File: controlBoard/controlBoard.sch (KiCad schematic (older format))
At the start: 18 parts, among them J1 FTDI, J2 Servo, J3 Fingerprint, J4 Barrel_Jack_Switch_MountingPin, J5 ICSP, SW1 SW_Push, SW2 SW_Push, SW3 SW_Push, U4 ATmega328P-AU, U5 PCA9685BS, Y1 Crystal

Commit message: Added button footprint and layout pcb
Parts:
- removed R1, R2: 10k, Resistor_SMD:R_0805_2012Metric_Pad1.20x1.40mm_HandSolder, symbol device:R_Small
- added C1, C2: 100n, Capacitor_SMD:C_0805_2012Metric_Pad1.18x1.45mm_HandSolder, symbol Device:C_Small
- added JP1: JVCC, Jumper:SolderJumper-2_P1.3mm_Open_RoundedPad1.0x1.5mm, symbol Jumper:SolderJumper_2_Open
- C3: renamed from C1; symbol device:C_Small -> controlBoard-rescue:C_Small-device
- C4: renamed from C2; symbol device:C_Small -> controlBoard-rescue:C_Small-device
- C5: renamed from C3; symbol device:C_Small -> controlBoard-rescue:C_Small-device
- C6: renamed from C4; symbol device:C_Small -> controlBoard-rescue:C_Small-device
- J3: footprint Connector_PinHeader_2.54mm:PinHeader_1x06_P2.54mm_Vertical -> Connector_JST:JST_PH_B6B-PH-K_1x06_P2.00mm_Vertical
- R3: renamed from R5; symbol device:R_Small -> controlBoard-rescue:R_Small-device
- SW1, SW2, SW3: footprint (none) -> bidpl:SMD_Pushbutton_3mmx4mm
- U1: renamed from U4; symbol MCU_Microchip_ATmega:ATmega328P-AU -> controlBoard-rescue:ATmega328P-AU-MCU_Microchip_ATmega
- Y1: footprint Crystal:Crystal_SMD_HC49-SD_HandSoldering -> Crystal:Crystal_SMD_5032-2Pin_5.0x3.2mm_HandSoldering; symbol device:Crystal -> controlBoard-rescue:Crystal-device
- renumbered U5 to U2
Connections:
- wire segments 96 -> 108

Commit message: Swapped TX1 and RX1 pins, cleaned up board a bit to send off to production
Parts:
- C1, C2: symbol Device:C_Small -> controlBoard-rescue:C_Small-Device
- J1, J3: symbol Connector_Generic:Conn_01x06 -> controlBoard-rescue:Conn_01x06-Connector_Generic
- J2: symbol Connector_Generic:Conn_01x03 -> controlBoard-rescue:Conn_01x03-Connector_Generic
- J4: symbol Connector:Barrel_Jack_Switch_MountingPin -> controlBoard-rescue:Barrel_Jack_Switch_MountingPin-Connector
- J5: symbol Connector_Generic:Conn_02x03_Odd_Even -> controlBoard-rescue:Conn_02x03_Odd_Even-Connector_Generic
- JP1: symbol Jumper:SolderJumper_2_Open -> controlBoard-rescue:SolderJumper_2_Open-Jumper
- SW1, SW2, SW3: symbol Switch:SW_Push -> controlBoard-rescue:SW_Push-Switch
- U2: symbol Driver_LED:PCA9685BS -> controlBoard-rescue:PCA9685BS-Driver_LED
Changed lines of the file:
@@
 $EndComp
 $Comp
-L power:GND #PWR017
+L controlBoard-rescue:GND-power #PWR017
 U 1 1 618DE613
 P 4200 5400
@@
 	4200 5300 4200 5400
 $Comp
-L power:+5V #PWR016
+L controlBoard-rescue:+5V-power #PWR016
 U 1 1 618E0ABB
 P 4200 2200
@@
 Connection ~ 4300 2250
 $Comp
-L power:GND #PWR018
+L controlBoard-rescue:GND-power #PWR018
 U 1 1 618E518F
 P 4800 2300
@@
 $EndComp
 $Comp
-L power:+5V #PWR019
+L controlBoard-rescue:+5V-power #PWR019
 U 1 1 618E816C
 P 5350 3750
@@
 	5350 4100 4800 4100
 $Comp
-L Switch:SW_Push SW3
+L controlBoard-rescue:SW_Push-Switch SW3
 U 1 1 618E9B97
 P 5900 4100
@@
 $EndComp
 $Comp
-L power:GND #PWR021
+L controlBoard-rescue:GND-power #PWR021
 U 1 1 618EA8D6
 P 6150 4150
@@
 	5850 3450 5650 3450
 $Comp
-L power:GND #PWR020
+L controlBoard-rescue:GND-power #PWR020
 U 1 1 618F026E
 P 5850 3550
@@
 	7700 4800 7700 4850
 $Comp
-L power:GND #PWR025
+L controlBoard-rescue:GND-power #PWR025
 U 1 1 618FA727
 P 7700 4900
@@
 Connection ~ 7700 4850
 $Comp
-L power:+5V #PWR024
+L controlBoard-rescue:+5V-power #PWR024
 U 1 1 618FB6AB
 P 7700 2600
@@
 	7700 2650 7700 2700
 $Comp
-L power:GND #PWR026
+L controlBoard-rescue:GND-power #PWR026
 U 1 1 61901090
 P 8300 2700
@@
 $EndComp
 $Comp
-L Driver_LED:PCA9685BS U2
+L controlBoard-rescue:PCA9685BS-Driver_LED U2
 U 1 1 618F6082
 P 7700 3700
@@
 F 1 "PCA9685BS" H 7400 4550 50  0000 C CNN
 F 2 "Package_DFN_QFN:QFN-28-1EP_6x6mm_P0.65mm_EP4.25x4.25mm" H 7725 2725 50  0001 L CNN
-F 3 "http://www.nxp.com/documents/data_sheet/PCA9685.pdf" H 7300 4400 50  0001 C CNN
+F 3 "https://www.nxp.com/docs/en/data-sheet/PCA9685.pdf" H 7300 4400 50  0001 C CNN
 	1    7700 3700
 	1    0    0    -1
@@
 	8300 2650 8300 2700
 $Comp
-L Switch:SW_Push SW1
+L controlBoard-rescue:SW_Push-Switch SW1
 U 1 1 6191D17B
 P 1350 5700
@@
 $EndComp
 $Comp
-L Switch:SW_Push SW2
+L controlBoard-rescue:SW_Push-Switch SW2
 U 1 1 6191DBBE
 P 1350 6750
@@
 $EndComp
 $Comp
-L power:GND #PWR08
+L controlBoard-rescue:GND-power #PWR08
 U 1 1 61922AC3
 P 1050 6850
@@
 $EndComp
 $Comp
-L power:GND #PWR07
+L controlBoard-rescue:GND-power #PWR07
 U 1 1 61922CB3
 P 1050 5800
@@
 $EndComp
 $Comp
-L Connector:Barrel_Jack_Switch_MountingPin J4
+L controlBoard-rescue:Barrel_Jack_Switch_MountingPin-Connector J4
 U 1 1 618E34A5
 P 1300 1150
@@
 $EndComp
 $Comp
-L Connector_Generic:Conn_02x03_Odd_Even J5
+L controlBoard-rescue:Conn_02x03_Odd_Even-Connector_Generic J5
 U 1 1 618EA8EC
 P 2450 2300
@@
 $EndComp
 $Comp
-L Connector_Generic:Conn_01x03 J2
+L controlBoard-rescue:Conn_01x03-Connector_Generic J2
 U 1 1 618ECDBF
 P 1050 3300
@@
 $EndComp
 $Comp
-L power:GND #PWR011
+L controlBoard-rescue:GND-power #PWR011
 U 1 1 618F500B
 P 1850 1500
@@
 	1600 1250 1850 1250
 $Comp
-L power:+5V #PWR012
+L controlBoard-rescue:+5V-power #PWR012
 U 1 1 619089DF
 P 2000 1000
@@
 	2000 1050 2000 1000
 $Comp
-L power:+5V #PWR013
+L controlBoard-rescue:+5V-power #PWR013
 U 1 1 6192E22C
 P 2800 2150
@@
 $EndComp
 $Comp
-L power:GND #PWR014
+L controlBoard-rescue:GND-power #PWR014
 U 1 1 6192F1F2
 P 2800 2450
@@
 	1250 3200 1600 3200
 $Comp
-L power:GND #PWR04
+L controlBoard-rescue:GND-power #PWR04
 U 1 1 61955E60
 P 1300 3450
@@
 	1300 3400 1300 3450
 $Comp
-L power:+5V #PWR010
+L controlBoard-rescue:+5V-power #PWR010
 U 1 1 61959E6E
 P 1750 3250
@@
 Text Label 8450 3000 0    50   ~ 0
 PWM0
-$Comp
-L Connector_Generic:Conn_01x06 J3
-U 1 1 61962843
-P 1050 4200
-F 0 "J3" H 968 4617 50  0000 C CNN
-F 1 "Fingerprint" H 968 4526 50  0000 C CNN
-F 2 "Connector_JST:JST_PH_B6B-PH-K_1x06_P2.00mm_Vertical" H 1050 4200 50  0001 C CNN
-F 3 "~" H 1050 4200 50  0001 C CNN
-	1    1050 4200
-	-1   0    0    -1
-$EndComp
-Wire Wire Line
-	1250 4400 1400 4400
-Wire Wire Line
-	1250 4300 1400 4300
-Wire Wire Line
-	1250 4200 1400 4200
-Wire Wire Line
-	1400 4200 1400 4150
-Wire Wire Line
-	1250 4500 1400 4500
-Wire Wire Line
-	1400 4500 1400 4550
-$Comp
-L power:GND #PWR06
-U 1 1 6197312B
-P 1400 4550
-F 0 "#PWR06" H 1400 4300 50  0001 C CNN
-F 1 "GND" H 1405 4377 50  0000 C CNN
-F 2 "" H 1400 4550 50  0001 C CNN
-F 3 "" H 1400 4550 50  0001 C CNN
-	1    1400 4550
-	1    0    0    -1
-$EndComp
-$Comp
-L power:+5V #PWR05
-U 1 1 61973A8E
-P 1400 4150
-F 0 "#PWR05" H 1400 4000 50  0001 C CNN
-F 1 "+5V" H 1415 4323 50  0000 C CNN
-F 2 "" H 1400 4150 50  0001 C CNN
-F 3 "" H 1400 4150 50  0001 C CNN
-	1    1400 4150
-	1    0    0    -1
-$EndComp
-Text Label 1250 4400 0    50   ~ 0
-RX1
-Text Label 1250 4300 0    50   ~ 0
-TX1
-NoConn ~ 1250 4100
-NoConn ~ 1250 4000
 Wire Wire Line
 	4800 4500 5000 4500
@@
 	4800 4600 5000 4600
 Text Label 4850 4500 0    50   ~ 0
+TX1
+Text Label 4850 4600 0    50   ~ 0
 RX1
-Text Label 4850 4600 0    50   ~ 0
-TX1
-$Comp
-L power:GND #PWR03
+$Comp
+L controlBoard-rescue:GND-power #PWR03
 U 1 1 6199143D
 P 1300 2750
@@
 RX
 $Comp
-L power:+5V #PWR09
+L controlBoard-rescue:+5V-power #PWR09
 U 1 1 6199F7F4
 P 1750 2450
@@
 	6800 3900 6800 4000
 $Comp
-L power:GND #PWR022
+L controlBoard-rescue:GND-power #PWR022
 U 1 1 61BB2179
 P 6800 4500
@@
 	6950 4400 7000 4400
 $Comp
-L power:+5V #PWR023
+L controlBoard-rescue:+5V-power #PWR023
 U 1 1 61BD1C2C
 P 6950 4400
@@
 $EndComp
 $Comp
-L Jumper:SolderJumper_2_Open JP1
+L controlBoard-rescue:SolderJumper_2_Open-Jumper JP1
 U 1 1 61BD91B4
 P 1550 2500
@@
 	1250 2500 1400 2500
 $Comp
-L Device:C_Small C1
+L controlBoard-rescue:C_Small-Device C1
 U 1 1 61BF76F9
 P 1500 2200
@@
 	1750 2500 1750 2450
 $Comp
-L Device:C_Small C2
+L controlBoard-rescue:C_Small-Device C2
 U 1 1 61C0D1ED
 P 3400 2600
@@
 $EndComp
 $Comp
-L power:GND #PWR015
+L controlBoard-rescue:GND-power #PWR015
 U 1 1 61C0E312
 P 3200 2700
@@
 	3200 2600 3300 2600
 $Comp
-L Connector_Generic:Conn_01x06 J1
+L controlBoard-rescue:Conn_01x06-Connector_Generic J1
 U 1 1 618EBBB2
 P 1050 2500
@@
 Wire Wire Line
 	1050 6750 1050 6850
+NoConn ~ 1250 4000
+NoConn ~ 1250 4100
+Text Label 1250 4300 0    50   ~ 0
+TX1
+Text Label 1250 4400 0    50   ~ 0
+RX1
+$Comp
+L controlBoard-rescue:+5V-power #PWR05
+U 1 1 61973A8E
+P 1400 4150
+F 0 "#PWR05" H 1400 4000 50  0001 C CNN
+F 1 "+5V" H 1415 4323 50  0000 C CNN
+F 2 "" H 1400 4150 50  0001 C CNN
+F 3 "" H 1400 4150 50  0001 C CNN
+	1    1400 4150
+	1    0    0    -1
+$EndComp
+$Comp
+L controlBoard-rescue:GND-power #PWR06
+U 1 1 6197312B
+P 1400 4550
+F 0 "#PWR06" H 1400 4300 50  0001 C CNN
+F 1 "GND" H 1405 4377 50  0000 C CNN
+F 2 "" H 1400 4550 50  0001 C CNN
+F 3 "" H 1400 4550 50  0001 C CNN
+	1    1400 4550
+	1    0    0    -1
+$EndComp
+Wire Wire Line
+	1400 4500 1400 4550
+Wire Wire Line
+	1250 4500 1400 4500
+Wire Wire Line
+	1400 4200 1400 4150
+Wire Wire Line
+	1250 4200 1400 4200
+Wire Wire Line
+	1250 4300 1400 4300
+Wire Wire Line
+	1250 4400 1400 4400
+$Comp
+L controlBoard-rescue:Conn_01x06-Connector_Generic J3
+U 1 1 61962843
+P 1050 4200
+F 0 "J3" H 968 4617 50  0000 C CNN
+F 1 "Fingerprint" H 968 4526 50  0000 C CNN
+F 2 "Connector_JST:JST_PH_B6B-PH-K_1x06_P2.00mm_Vertical" H 1050 4200 50  0001 C CNN
+F 3 "~" H 1050 4200 50  0001 C CNN
+	1    1050 4200
+	-1   0    0    -1
+$EndComp
 $EndSCHEMATC

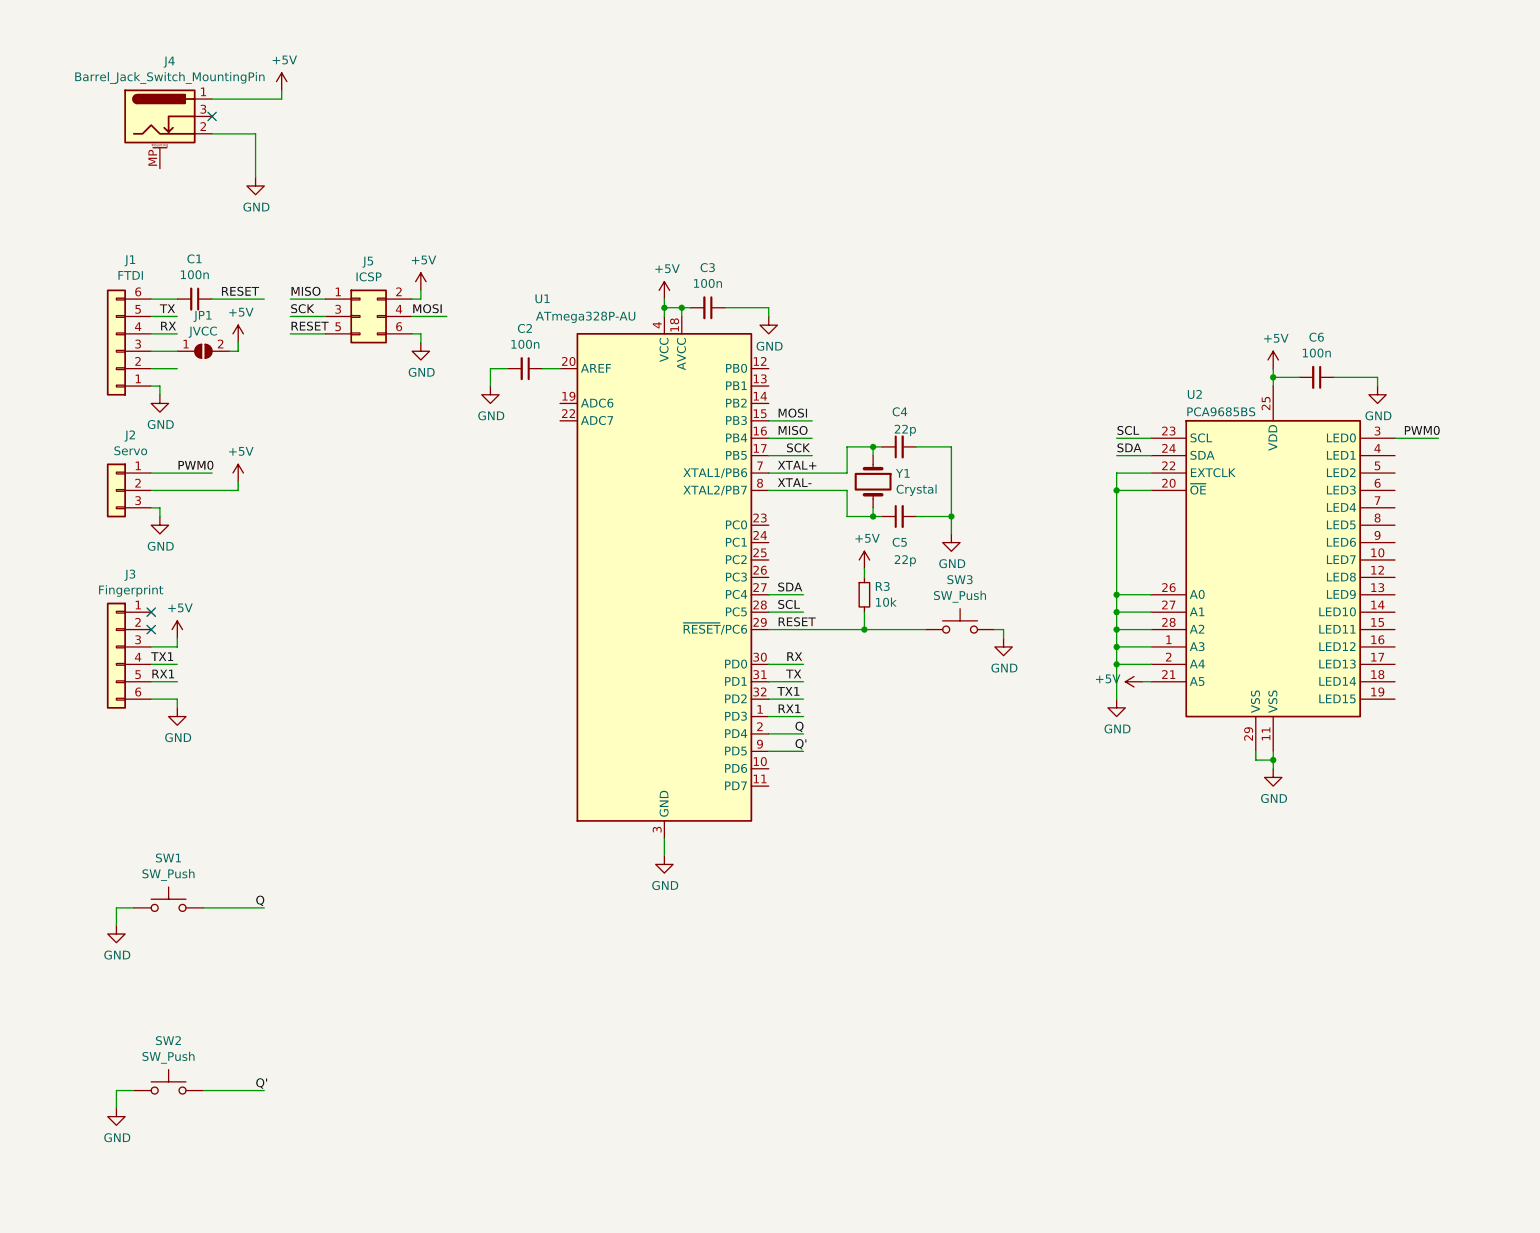
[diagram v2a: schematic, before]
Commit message: Added 2 electrolytic caps, pin 13 led, 3v3 linear reg, seperated power for logic and servo, increased board size, rotated some headers, added some test points
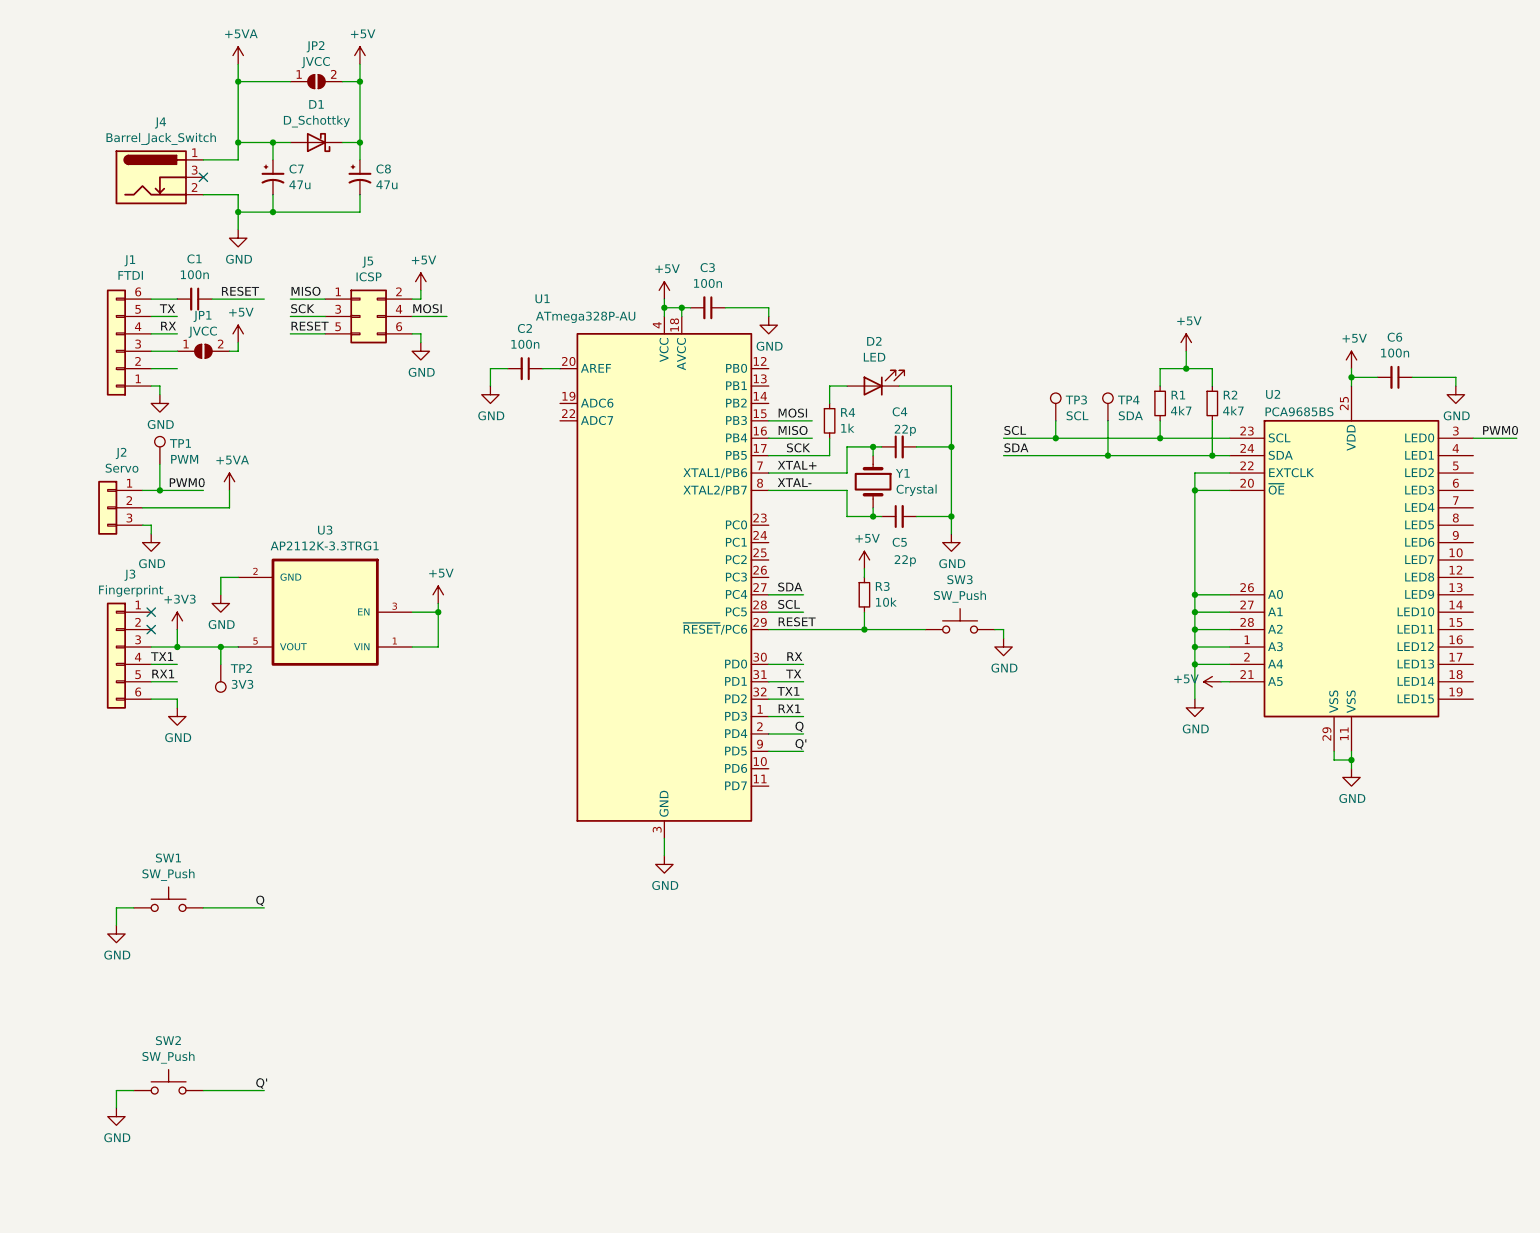
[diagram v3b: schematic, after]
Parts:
- removed J4: Barrel_Jack_Switch_MountingPin, Connector_BarrelJack:BarrelJack_Horizontal, symbol controlBoard-rescue:Barrel_Jack_Switch_MountingPin-Connector
- added C7, C8: 47u, Capacitor_SMD:CP_Elec_6.3x7.7, symbol Device:CP1_Small
- added D1: D_Schottky, Diode_SMD:D_SOD-123, symbol Device:D_Schottky
- added D2: LED, LED_SMD:LED_0805_2012Metric_Pad1.15x1.40mm_HandSolder, symbol Device:LED
- added J4: Barrel_Jack_Switch, Connector_BarrelJack:BarrelJack_Horizontal, symbol Connector:Barrel_Jack_Switch
- added JP2: JVCC, Jumper:SolderJumper-2_P1.3mm_Open_RoundedPad1.0x1.5mm, symbol controlBoard-rescue:SolderJumper_2_Open-Jumper
- added R1, R2: 4k7, Resistor_SMD:R_0805_2012Metric_Pad1.20x1.40mm_HandSolder, symbol Device:R_Small
- added R4: 1k, Resistor_SMD:R_0805_2012Metric_Pad1.20x1.40mm_HandSolder, symbol Device:R_Small
- added TP1: PWM, TestPoint:TestPoint_Pad_D1.5mm, symbol Connector:TestPoint
- added TP2: 3V3, TestPoint:TestPoint_Pad_D1.5mm, symbol Connector:TestPoint
- added TP3: SCL, TestPoint:TestPoint_Pad_D1.5mm, symbol Connector:TestPoint
- added TP4: SDA, TestPoint:TestPoint_Pad_D1.5mm, symbol Connector:TestPoint
- added U3: AP2112K-3.3TRG1, SOT95P285X140-5N, symbol AP2112K-3.3TRG1:AP2112K-3.3TRG1
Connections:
- net labels added: +3V3, +5VA
- wire segments 108 -> 153
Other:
- moved on the sheet: C6, J2, U2
